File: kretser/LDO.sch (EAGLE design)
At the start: 5 parts, among them U2 LM2940CT-5.0/NOPB

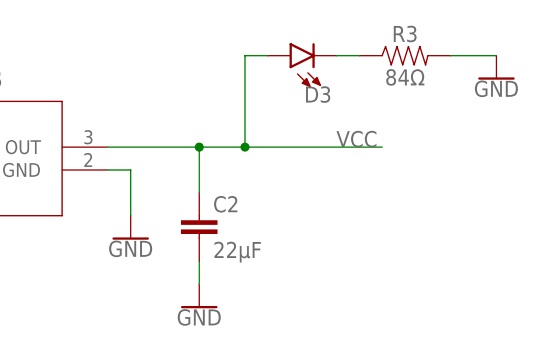
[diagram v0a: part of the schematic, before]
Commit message: Changed LDO Resistor value to 330 [Ohm]
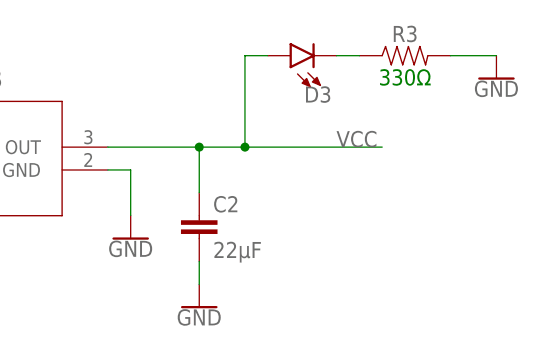
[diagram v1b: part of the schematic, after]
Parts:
- R3: value 84Ω -> 330Ω
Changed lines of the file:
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@@
 <part name="GND8" library="SparkFun-PowerSymbols" library_urn="urn:adsk.eagle:library:530" deviceset="GND" device=""/>
 <part name="D3" library="SparkFun-LED" library_urn="urn:adsk.eagle:library:529" deviceset="LED" device="5MM" package3d_urn="urn:adsk.eagle:package:39353/2"/>
-<part name="R3" library="SparkFun-Resistors" library_urn="urn:adsk.eagle:library:532" deviceset="10OHM" device="-HORIZ-1/4W-1%" package3d_urn="urn:adsk.eagle:package:39658/2" value="84Ω"/>
+<part name="R3" library="SparkFun-Resistors" library_urn="urn:adsk.eagle:library:532" deviceset="10OHM" device="-HORIZ-1/4W-1%" package3d_urn="urn:adsk.eagle:package:39658/2" value="330Ω"/>
 </parts>
 <sheets>
@@
 <instance part="R3" gate="G$1" x="172.72" y="116.84" smashed="yes">
 <attribute name="NAME" x="172.72" y="118.364" size="1.778" layer="95" font="vector" align="bottom-center"/>
-<attribute name="VALUE" x="172.72" y="115.316" size="1.778" layer="96" font="vector" align="top-center"/>
+<attribute name="VALUE" x="172.72" y="115.316" size="1.778" layer="91" font="vector" align="top-center"/>
 </instance>
 </instances>

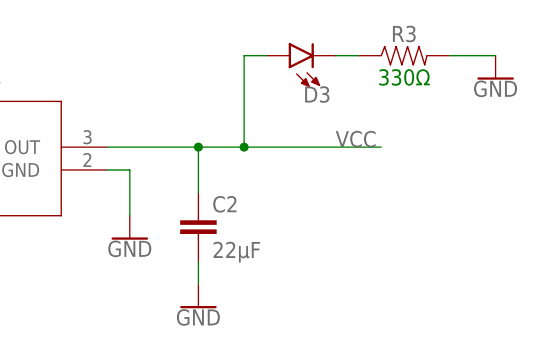
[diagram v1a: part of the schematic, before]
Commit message: Un-blue'd resistor value. I don't like Eagle.
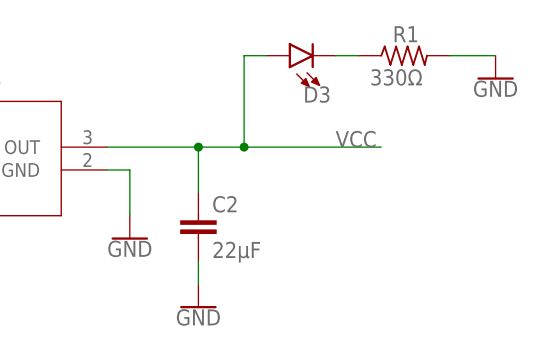
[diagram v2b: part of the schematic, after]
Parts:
- removed R3: 330Ω, SparkFun-Resistors:10OHM-HORIZ-1/4W-1%
- added R1: 330Ω, rcl:R-US_0207/2V
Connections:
- net GND: now also R1.2; no longer R3.2
- net N$6: now also R1.1; no longer R3.1
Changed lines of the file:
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@@
 <part name="GND8" library="SparkFun-PowerSymbols" library_urn="urn:adsk.eagle:library:530" deviceset="GND" device=""/>
 <part name="D3" library="SparkFun-LED" library_urn="urn:adsk.eagle:library:529" deviceset="LED" device="5MM" package3d_urn="urn:adsk.eagle:package:39353/2"/>
-<part name="R3" library="SparkFun-Resistors" library_urn="urn:adsk.eagle:library:532" deviceset="10OHM" device="-HORIZ-1/4W-1%" package3d_urn="urn:adsk.eagle:package:39658/2" value="330Ω"/>
+<part name="R1" library="rcl" library_urn="urn:adsk.eagle:library:334" deviceset="R-US_" device="0207/2V" package3d_urn="urn:adsk.eagle:package:23490/1" value="330Ω"/>
 </parts>
 <sheets>
@@
 <attribute name="VALUE" x="164.592" y="118.745" size="1.778" layer="96" font="vector" rot="R180" align="top-left"/>
 </instance>
-<instance part="R3" gate="G$1" x="172.72" y="116.84" smashed="yes">
-<attribute name="NAME" x="172.72" y="118.364" size="1.778" layer="95" font="vector" align="bottom-center"/>
-<attribute name="VALUE" x="172.72" y="115.316" size="1.778" layer="91" font="vector" align="top-center"/>
+<instance part="R1" gate="G$1" x="172.72" y="116.84" smashed="yes">
+<attribute name="NAME" x="171.45" y="118.3386" size="1.778" layer="95"/>
+<attribute name="VALUE" x="168.91" y="113.538" size="1.778" layer="96"/>
 </instance>
 </instances>
@@
 </segment>
 <segment>
-<pinref part="R3" gate="G$1" pin="2"/>
 <pinref part="GND8" gate="1" pin="GND"/>
 <wire x1="182.88" y1="116.84" x2="177.8" y2="116.84" width="0.1524" layer="91"/>
+<pinref part="R1" gate="G$1" pin="2"/>
 </segment>
 </net>
@@
 <segment>
 <pinref part="D3" gate="D1" pin="C"/>
-<pinref part="R3" gate="G$1" pin="1"/>
 <wire x1="165.1" y1="116.84" x2="167.64" y2="116.84" width="0.1524" layer="91"/>
+<pinref part="R1" gate="G$1" pin="1"/>
 </segment>
 </net>
@@
 packages will not be understood (or retained) with this version.
 </note>
+<note version="8.4" severity="warning">
+Since Version 8.4, EAGLE supports properties for SPICE simulation.
+Probes in schematics and SPICE mapping objects found in parts and library devices
+will not be understood with this version. Update EAGLE to the latest version
+for full support of SPICE simulation.
+</note>
 </compatibility>

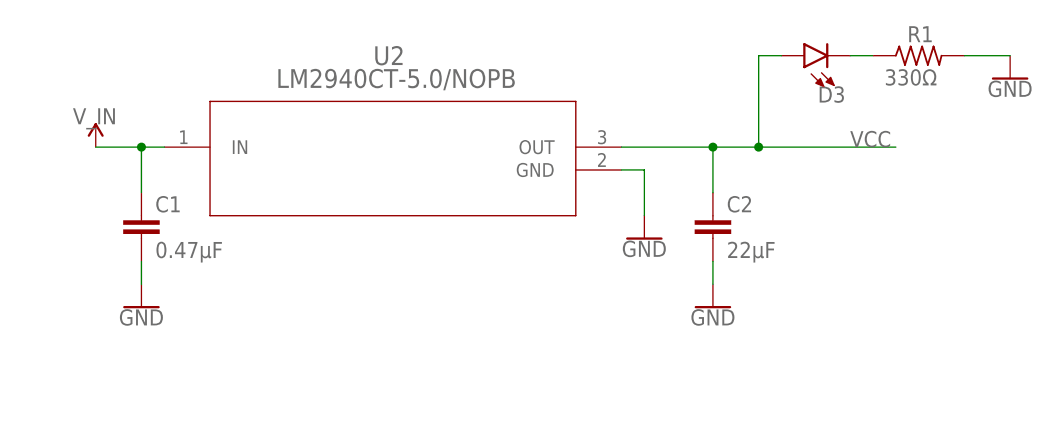
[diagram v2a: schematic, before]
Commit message: Fixed Capacitor parallel connection & resistor value 84 to 330 on main circuit.
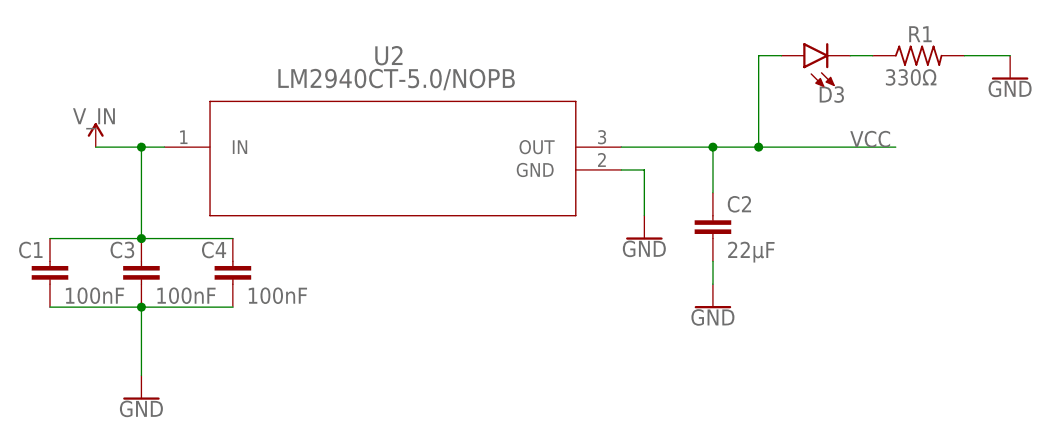
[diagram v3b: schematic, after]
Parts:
- added C3, C4: 100nF, SparkFun-Capacitors:470PF-0603-50V-5%
- C1: value 0.47µF -> 100nF
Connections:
- net GND: now also C3.2, C4.2
- net V_IN: now also C3.1, C4.1
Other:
- moved on the sheet: C1
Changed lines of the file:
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@@
 </part>
 <part name="SUPPLY1" library="SparkFun-PowerSymbols" library_urn="urn:adsk.eagle:library:530" deviceset="VCC" device=""/>
-<part name="C1" library="SparkFun-Capacitors" library_urn="urn:adsk.eagle:library:510" deviceset="470PF" device="-0603-50V-5%" package3d_urn="urn:adsk.eagle:package:41385090/1" value="0.47µF">
+<part name="C1" library="SparkFun-Capacitors" library_urn="urn:adsk.eagle:library:510" deviceset="470PF" device="-0603-50V-5%" package3d_urn="urn:adsk.eagle:package:41385090/1" value="100nF">
 <attribute name="SPICEPREFIX" value="C"/>
 </part>
@@
 <part name="D3" library="SparkFun-LED" library_urn="urn:adsk.eagle:library:529" deviceset="LED" device="5MM" package3d_urn="urn:adsk.eagle:package:39353/2"/>
 <part name="R1" library="rcl" library_urn="urn:adsk.eagle:library:334" deviceset="R-US_" device="0207/2V" package3d_urn="urn:adsk.eagle:package:23490/1" value="330Ω"/>
+<part name="C3" library="SparkFun-Capacitors" library_urn="urn:adsk.eagle:library:510" deviceset="470PF" device="-0603-50V-5%" package3d_urn="urn:adsk.eagle:package:41385090/1" value="100nF">
+<attribute name="SPICEPREFIX" value="C"/>
+</part>
+<part name="C4" library="SparkFun-Capacitors" library_urn="urn:adsk.eagle:library:510" deviceset="470PF" device="-0603-50V-5%" package3d_urn="urn:adsk.eagle:package:41385090/1" value="100nF">
+<attribute name="SPICEPREFIX" value="C"/>
+</part>
 </parts>
 <sheets>
@@
 <attribute name="VALUE" x="101.3206" y="113.2586" size="2.0828" layer="96" ratio="6" rot="SR0"/>
 </instance>
-<instance part="GND1" gate="1" x="86.36" y="88.9" smashed="yes">
-<attribute name="VALUE" x="86.36" y="88.646" size="1.778" layer="96" font="vector" align="top-center"/>
+<instance part="GND1" gate="1" x="86.36" y="78.74" smashed="yes">
+<attribute name="VALUE" x="86.36" y="78.486" size="1.778" layer="96" font="vector" align="top-center"/>
 </instance>
 <instance part="GND2" gate="1" x="142.24" y="96.52" smashed="yes">
@@
 </instance>
 <instance part="SUPPLY1" gate="G$1" x="81.28" y="106.68" smashed="yes"/>
-<instance part="C1" gate="G$1" x="86.36" y="96.52" smashed="yes">
-<attribute name="NAME" x="87.884" y="99.441" size="1.778" layer="95" font="vector"/>
-<attribute name="VALUE" x="87.884" y="94.361" size="1.778" layer="96" font="vector"/>
+<instance part="C1" gate="G$1" x="76.2" y="91.44" smashed="yes">
+<attribute name="NAME" x="72.644" y="94.361" size="1.778" layer="95" font="vector"/>
+<attribute name="VALUE" x="77.724" y="89.281" size="1.778" layer="96" font="vector"/>
 </instance>
 <instance part="C2" gate="G$1" x="149.86" y="96.52" smashed="yes">
@@
 <attribute name="VALUE" x="168.91" y="113.538" size="1.778" layer="96"/>
 </instance>
+<instance part="C3" gate="G$1" x="86.36" y="91.44" smashed="yes">
+<attribute name="NAME" x="82.804" y="94.361" size="1.778" layer="95" font="vector"/>
+<attribute name="VALUE" x="87.884" y="89.281" size="1.778" layer="96" font="vector"/>
+</instance>
+<instance part="C4" gate="G$1" x="96.52" y="91.44" smashed="yes">
+<attribute name="NAME" x="92.964" y="94.361" size="1.778" layer="95" font="vector"/>
+<attribute name="VALUE" x="98.044" y="89.281" size="1.778" layer="96" font="vector"/>
+</instance>
 </instances>
 <busses>
@@
 <pinref part="SUPPLY1" gate="G$1" pin="VCC"/>
 <pinref part="U2" gate="A" pin="IN"/>
+<wire x1="81.28" y1="106.68" x2="86.36" y2="106.68" width="0.1524" layer="91"/>
+<label x="78.74" y="109.22" size="1.778" layer="95"/>
+<pinref part="C4" gate="G$1" pin="1"/>
+<pinref part="C3" gate="G$1" pin="1"/>
+<wire x1="86.36" y1="106.68" x2="88.9" y2="106.68" width="0.1524" layer="91"/>
+<wire x1="96.52" y1="96.52" x2="86.36" y2="96.52" width="0.1524" layer="91"/>
 <pinref part="C1" gate="G$1" pin="1"/>
-<wire x1="81.28" y1="106.68" x2="86.36" y2="106.68" width="0.1524" layer="91"/>
-<wire x1="86.36" y1="106.68" x2="88.9" y2="106.68" width="0.1524" layer="91"/>
-<wire x1="86.36" y1="101.6" x2="86.36" y2="106.68" width="0.1524" layer="91"/>
+<wire x1="86.36" y1="96.52" x2="76.2" y2="96.52" width="0.1524" layer="91"/>
+<junction x="86.36" y="96.52"/>
+<wire x1="86.36" y1="96.52" x2="86.36" y2="106.68" width="0.1524" layer="91"/>
 <junction x="86.36" y="106.68"/>
-<label x="78.74" y="109.22" size="1.778" layer="95"/>
 </segment>
 </net>
 <net name="GND" class="0">
-<segment>
-<pinref part="GND1" gate="1" pin="GND"/>
-<pinref part="C1" gate="G$1" pin="2"/>
-<wire x1="86.36" y1="91.44" x2="86.36" y2="93.98" width="0.1524" layer="91"/>
-</segment>
 <segment>
 <pinref part="GND2" gate="1" pin="GND"/>
@@
 <pinref part="R1" gate="G$1" pin="2"/>
 </segment>
+<segment>
+<pinref part="C4" gate="G$1" pin="2"/>
+<pinref part="C3" gate="G$1" pin="2"/>
+<wire x1="96.52" y1="88.9" x2="86.36" y2="88.9" width="0.1524" layer="91"/>
+<pinref part="GND1" gate="1" pin="GND"/>
+<wire x1="86.36" y1="88.9" x2="86.36" y2="81.28" width="0.1524" layer="91"/>
+<junction x="86.36" y="88.9"/>
+<pinref part="C1" gate="G$1" pin="2"/>
+<wire x1="86.36" y1="88.9" x2="76.2" y2="88.9" width="0.1524" layer="91"/>
+</segment>
 </net>
